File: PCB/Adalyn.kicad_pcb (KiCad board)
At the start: 2 copper layers, 217.7 x 85.3 mm, 76 parts, among them SW1 SW_Push, U101 ATmega32U4-A, U102 PRTR5V0U2X, Y1 16MHz

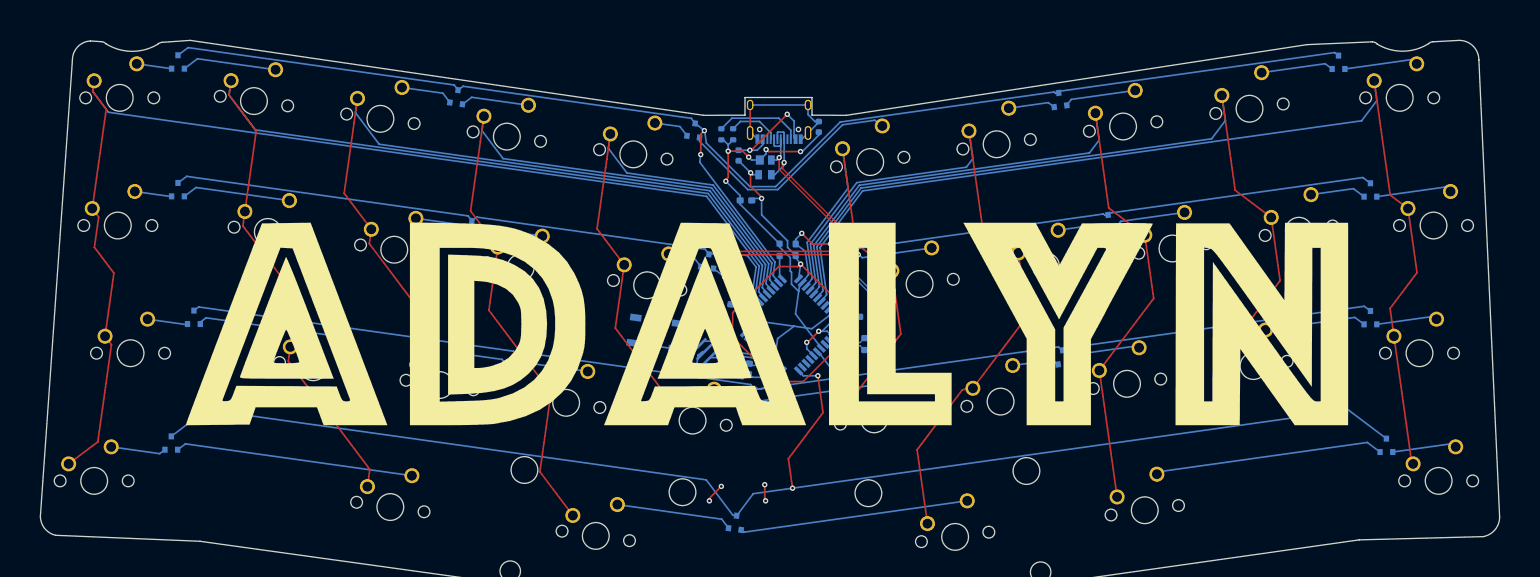
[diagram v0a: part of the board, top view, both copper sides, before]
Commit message: BOM + CPL for JLCPCB
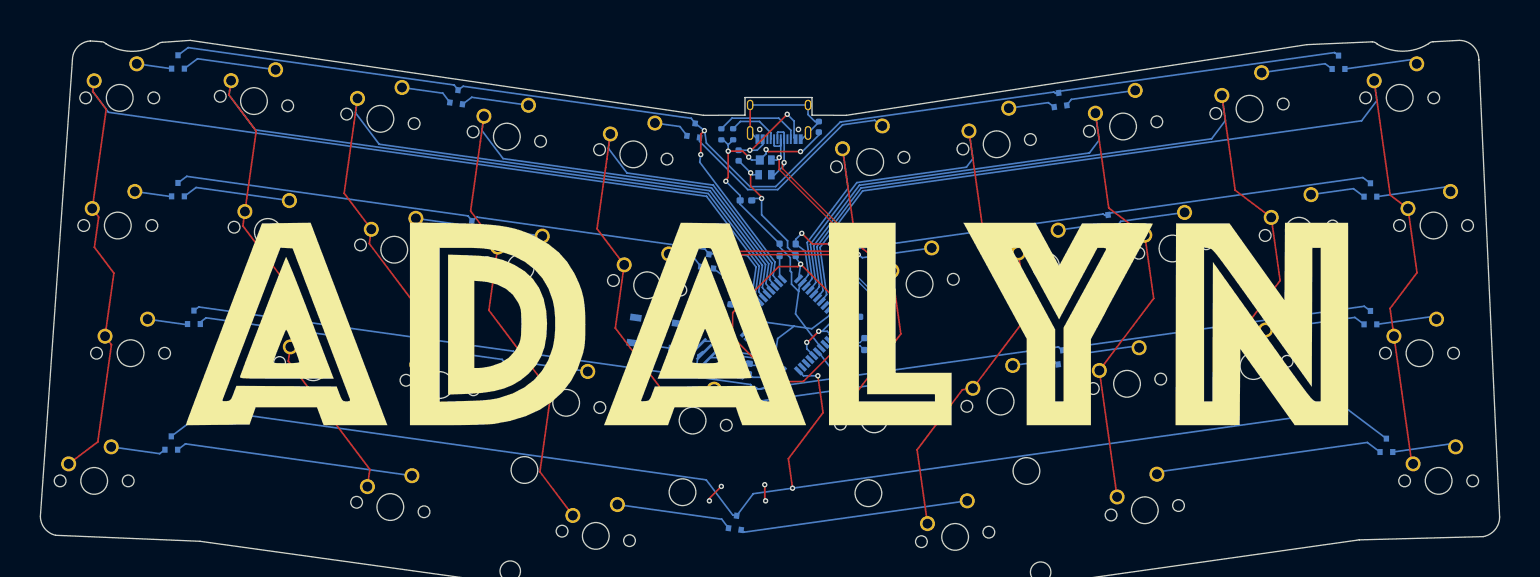
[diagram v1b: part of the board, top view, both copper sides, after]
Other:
- net class Default removed
